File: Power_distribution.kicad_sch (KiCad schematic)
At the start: 15 parts, among them U10 MP2491C, U11 AMS1117-3.3, U14 MIC2026-1xM, U15 MIC2026-1xM, U17 MIC2026-1xM, U9 MP2491C

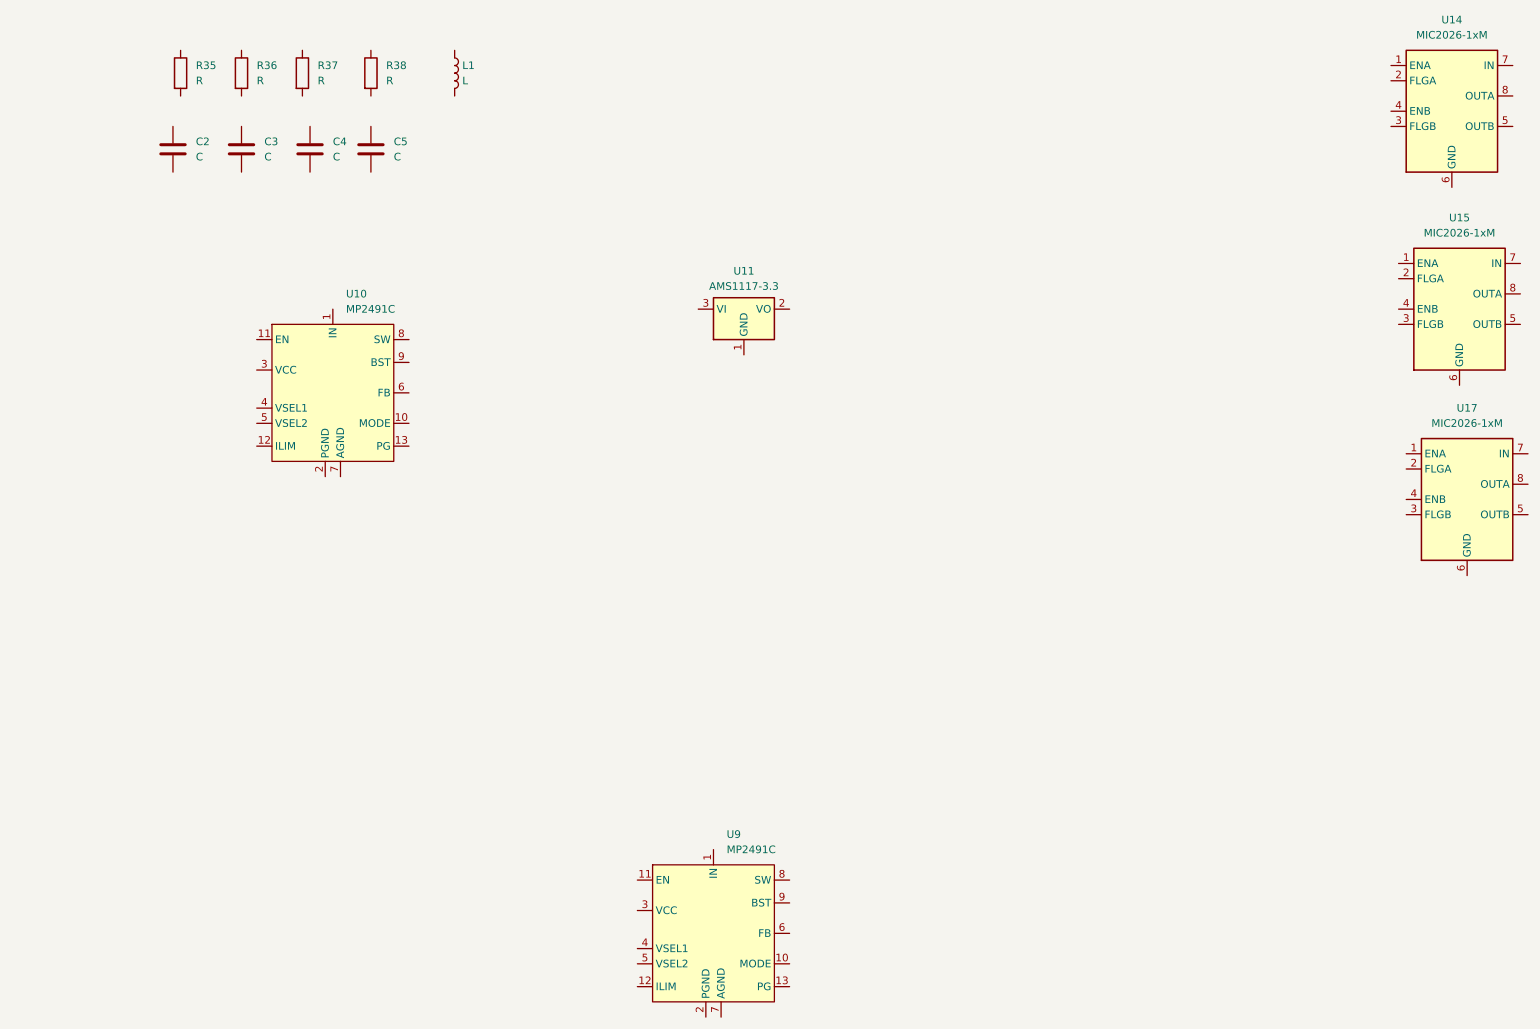
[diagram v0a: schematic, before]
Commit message: Power schematic update of one DC/DC converter
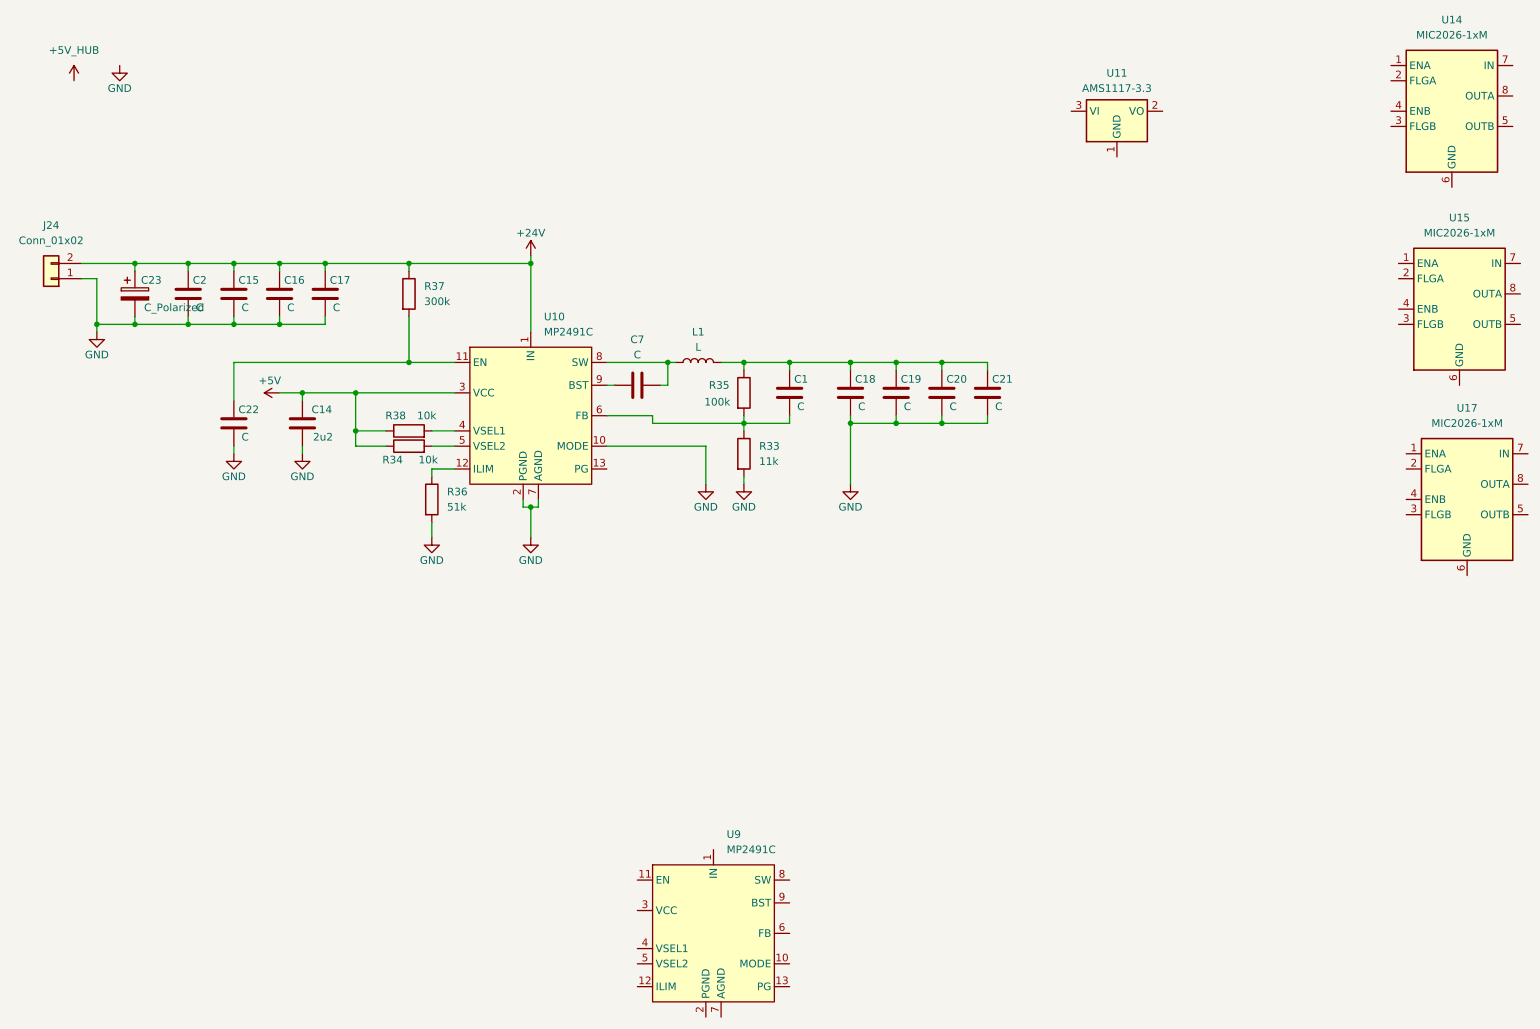
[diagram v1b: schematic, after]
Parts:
- removed C3, C4, C5: C, symbol Device:C
- added C1, C15, C16, C17, C18, C19, C20, C21, C22, C7: C, symbol Device:C
- added C14: 2u2, symbol Device:C
- added C23: C_Polarized, symbol Device:C_Polarized
- added J24: Conn_01x02, Connector_Phoenix_MSTB:PhoenixContact_MSTBA_2,5_2-G_1x02_P5.00mm_Horizontal, symbol Connector_Generic:Conn_01x02
- added R33: 11k, symbol Device:R
- added R34: 10k, symbol Device:R
- R35: value R -> 100k
- R36: value R -> 51k
- R37: value R -> 300k
- R38: value R -> 10k
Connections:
- net +5V: now reaches R38.1
- net +5V: now also U10.3 (VCC), C14.1, R34.1
- net at R38.2: now also U10.4 (VSEL1)
- net at R36.1: now also U10.12 (ILIM)
- net GND: now reaches R36.2
- net GND: now also C2.2, U10.10 (MODE), U10.2 (PGND), U10.7 (AGND), C14.2, C15.2, C16.2, C17.2, C18.2, C19.2, C20.2, C21.2, C22.2, C23.2, J24.1 (Pin_1), R33.2
- net at R35.1: now also L1.2, C1.1, C18.1, C19.1, C20.1, C21.1
- net at R35.2: now also U10.6 (FB), C1.2, R33.1
- net +24V: now reaches U10.1 (IN)
- net +24V: now also C2.1, R37.1, C15.1, C16.1, C17.1, C23.1, J24.2 (Pin_2)
- net at U10.11 (EN): now also R37.2, C22.1
- net at U10.5 (VSEL2): now also R34.2
- net at U10.8 (SW): now also L1.1, C7.1
- net at U10.9 (BST): now also C7.2
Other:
- moved on the sheet: C2, L1, R35, R36, R37, U10, U11

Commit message: Added values for passive elements near DC/DC
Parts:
- added R39, R40: 0, symbol Device:R
- added R41: 10k, symbol Device:R
- C1: value C -> 22p
- C15, C16, C2: value C -> 10u
- C17: value C -> 100n
- C18, C19, C20, C21: value C -> 22u
- C22: value C -> 1n
- C23: value C_Polarized -> 100u
- C7: value C -> 1u
- L1: value L -> 4u7
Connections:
- net +5V: now also R41.2
- net GND: now also R40.2; no longer U10.10 (MODE)
- net at U10.13 (PG): now also R41.1
- net at U10.9 (BST): now also R39.1; no longer C7.2
- new net: R40.1, U10.10 (MODE)
- new net: C7.2, R39.2
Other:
- moved on the sheet: C1, C15, C16, C17, C18, C19, C2, C20, C21, C23, C7, J24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
